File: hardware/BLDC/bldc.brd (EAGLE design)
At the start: 51 x 40 mm, 28 parts, among them U1 MA702, U2 DRV8323RS, U3 TPN7R006PL, U4 TPN7R006PL, U5 TPN7R006PL, U6 TPN7R006PL, U7 TPN7R006PL, U8 TPN7R006PL, U9 STM32G4_UFQFPN48_T1

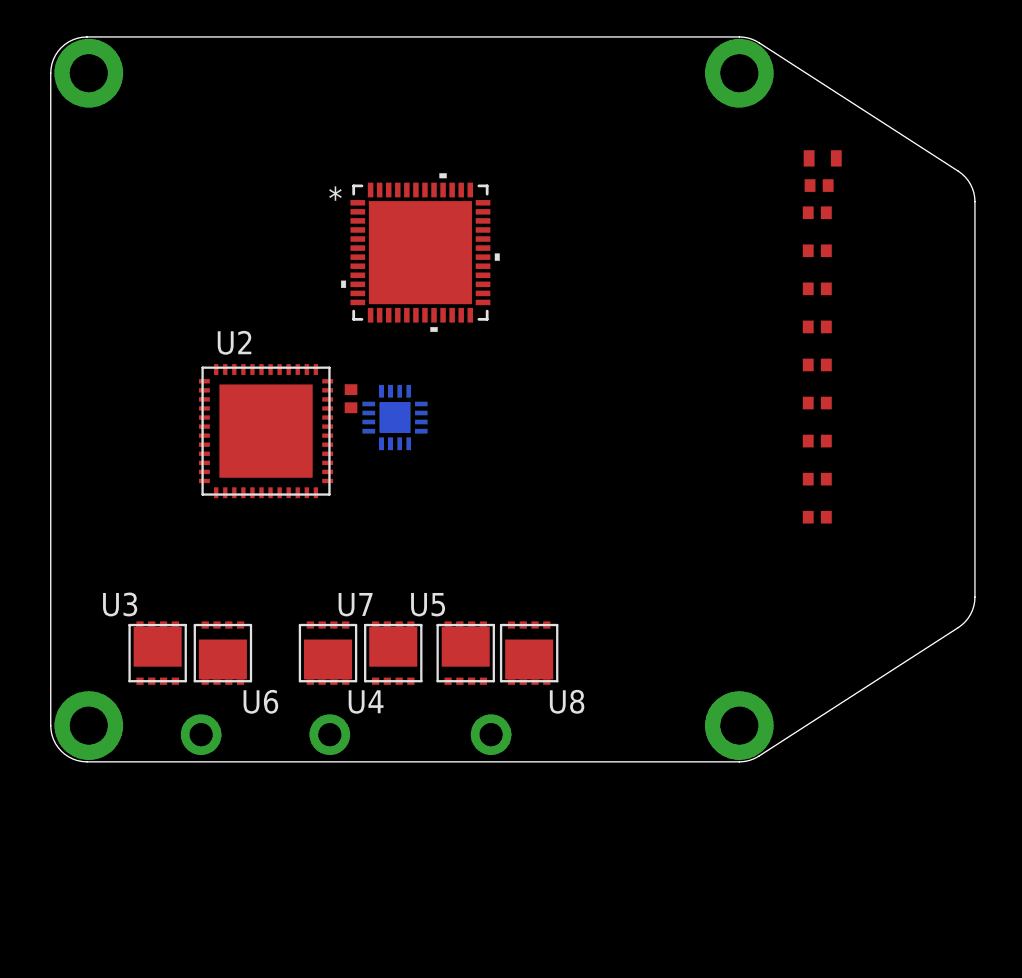
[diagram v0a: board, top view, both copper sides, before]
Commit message: Mostly updates to add inductor
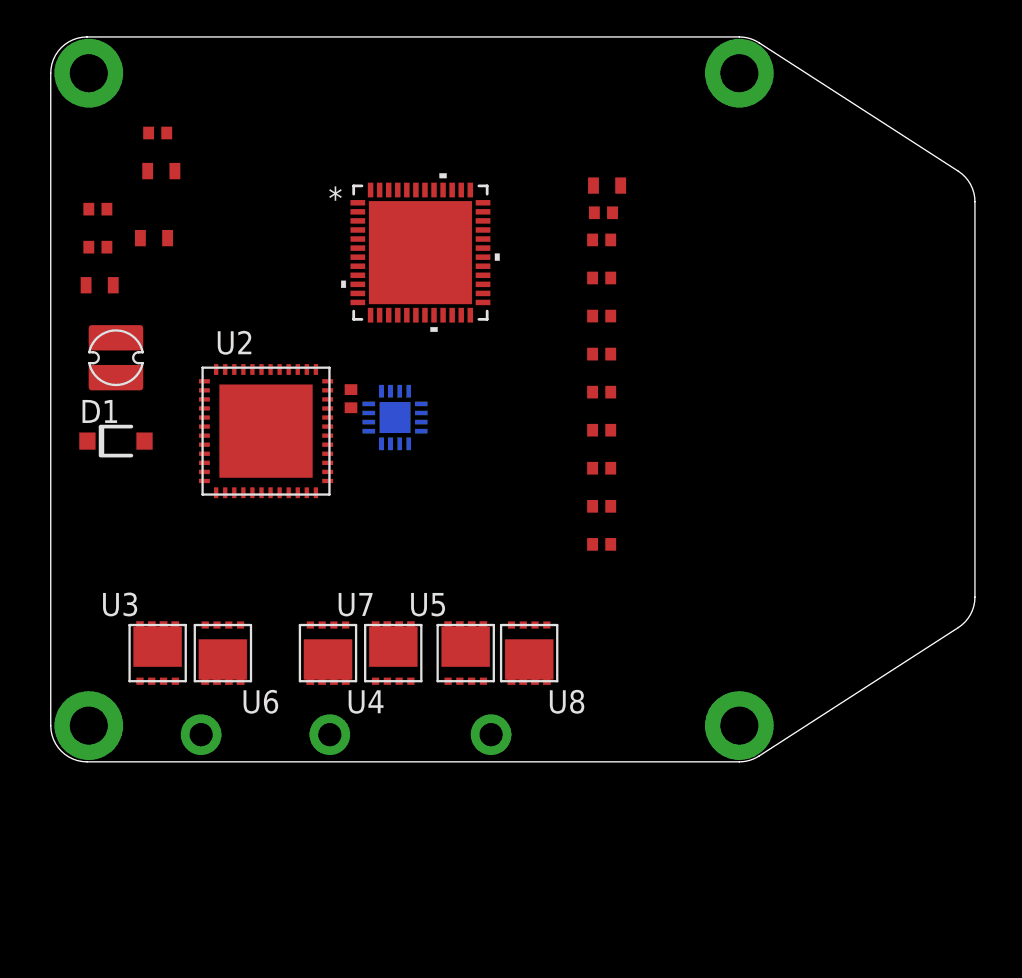
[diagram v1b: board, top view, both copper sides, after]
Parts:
- added C12, C14: 2.2uF 50V, _T_rcl:C0603
- added C13: 100nF 10V, _T_rcl:C0603
- added D1: SCHOTTKY_SOD123, _T_rcl:SOD123
- added L2: 22uH Bourns, _T_rcl:SDR0302
- added R1, R2, R3: 100k, _T_rcl:R0402
- moved L1 12.0 mm to (30.7, 31.8)
- moved C10 12.0 mm to (30.4, 14.1)
- moved C11 12.0 mm to (30.4, 12.0)
- moved C2 12.0 mm to (30.5, 30.3)
- moved C3 12.0 mm to (30.4, 28.8)
- moved C4 12.0 mm to (30.4, 26.7)
- moved C5 12.0 mm to (30.4, 24.6)
- moved C6 12.0 mm to (30.4, 22.5)
- moved C7 12.0 mm to (30.4, 20.4)
- moved C8 12.0 mm to (30.4, 18.3)
- moved C9 12.0 mm to (30.4, 16.2)
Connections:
- removed net GND: C1.2, C10.2, C11.2, C4.2, C5.2, C6.2, C7.2, C8.2, C9.2, H1.PAD, H2.PAD, H3.PAD, H4.PAD, U1.10, U1.8, U1.PAD, U2.38, U2.40, U2.42, U9.49
- new net N#8: C1.2, C10.2, C11.2, C12.2, C14.2, C4.2, C5.2, C6.2, C7.2, C8.2, C9.2, D1.A, H1.PAD, H2.PAD, H3.PAD, H4.PAD, R3.1, U1.10, U1.8, U1.PAD, U2.38, U2.40, U2.42, U2.43, U9.49
- new net N$10: C14.1, L2.PIN2, R2.2
- new net N$5: R1.2, U2.48
- new net N$6: C13.1, U2.44
- new net N$8: C13.2, D1.C, L2.PIN1, U2.45
- new net N$9: R2.1, R3.2, U2.1
- net +3V3: now also C12.1, R1.1, U2.47
- net N$2: now also U3.SOURCE, U3.SOURCE@1, U3.SOURCE@2, U6.DRAIN; no longer U3.PIN1, U3.PIN2, U3.PIN3, U6.PIN5, U6.PIN6, U6.PIN7, U6.PIN8
- net N$3: now also U4.SOURCE, U4.SOURCE@1, U4.SOURCE@2, U7.DRAIN; no longer U4.PIN1, U4.PIN2, U4.PIN3, U7.PIN5, U7.PIN6, U7.PIN7, U7.PIN8
- net N$4: now also U5.SOURCE, U5.SOURCE@1, U5.SOURCE@2, U8.DRAIN; no longer U5.PIN1, U5.PIN2, U5.PIN3, U8.PIN5, U8.PIN6, U8.PIN7, U8.PIN8

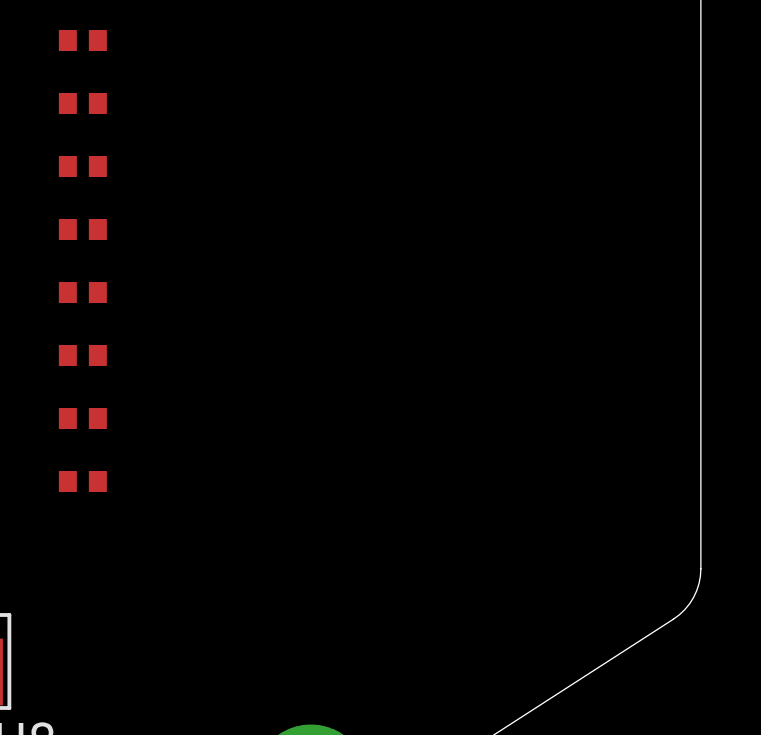
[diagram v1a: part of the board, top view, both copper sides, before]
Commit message: Added xt30
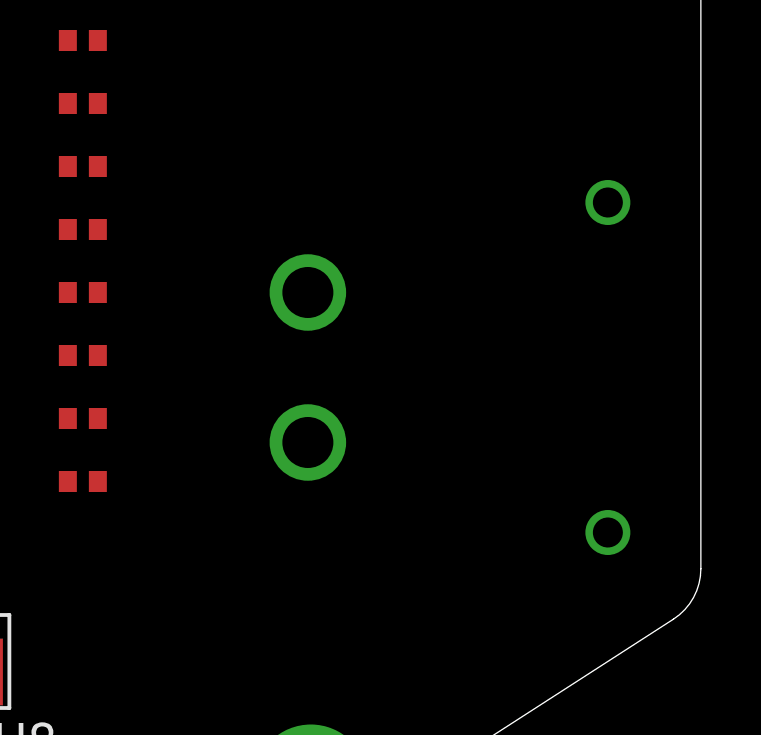
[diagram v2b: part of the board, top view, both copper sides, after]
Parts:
- added J1: PWR_2_XT30PW-M, _T_conn:XT30PW-M
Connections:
- new net +24V: C12.1, J1.P$1, R1.1, U2.47
- new net GND: J1.P$2
- net +3V3: no longer C12.1, R1.1, U2.47
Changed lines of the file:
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@@
 </layers>
 <board>
-<fusionsync huburn="a.YnVzaW5lc3M6Z21haWwyMjE5MTc" projecturn="a.YnVzaW5lc3M6Z21haWwyMjE5MTcjMjAxOTA2MjkyMDE0MTU5NzY" f3durn="urn:adsk.wipprod:dm.lineage:e4urj2y-ReajaBtUk_DaUw" pcbguid="" lastpulledtime="2020-05-16T20:54:00Z" lastsyncedchangeguid="" latestrevisionid="6bcccb4f-ea81-44fc-9b3c-a914c7c98af3" lastsyncedrevisionid="6bcccb4f-ea81-44fc-9b3c-a914c7c98af3" lastboardhashguid="70862e9e-f1a5-705a-7dcf-818cbcfc4620" lastpushedtime="2020-05-17T06:26:25Z" linktopcb3d="%12"/>
+<fusionsync huburn="a.YnVzaW5lc3M6Z21haWwyMjE5MTc" projecturn="a.YnVzaW5lc3M6Z21haWwyMjE5MTcjMjAxOTA2MjkyMDE0MTU5NzY" f3durn="urn:adsk.wipprod:dm.lineage:e4urj2y-ReajaBtUk_DaUw" pcbguid="" lastpulledtime="2020-05-16T20:54:00Z" lastsyncedchangeguid="" latestrevisionid="02e32407-8d36-474b-8d24-b2379baf0c01" lastsyncedrevisionid="02e32407-8d36-474b-8d24-b2379baf0c01" lastboardhashguid="b426c96d-69ff-6449-4c27-9cbcb447e0c3" lastpushedtime="2020-05-17T07:07:59Z" linktopcb3d="%12"/>
 <plain>
 <wire x1="39.0836" y1="39.681" x2="38" y2="40" width="0" layer="20" curve="32.8049"/>
@@
 </element>
 <element name="C1" library="_T_rcl" library_urn="urn:adsk.eagle:library:19571919" package="C0402" package3d_urn="urn:adsk.eagle:package:19572013/3" value="1uf 10v" x="16.57" y="20.04" smashed="yes" rot="R90"/>
-<element name="U4" library="_T_transistors" library_urn="urn:adsk.eagle:library:19605452" package="2-3X1S-TSONADVANCE" package3d_urn="urn:adsk.eagle:package:20292156/2" value="TPN7R006PL" x="15.3" y="6" smashed="yes" rot="R180">
+<element name="U4" library="_T_transistors" library_urn="urn:adsk.eagle:library:19605452" package="2-3X1S-TSONADVANCE" package3d_urn="urn:adsk.eagle:package:20292156/3" value="TPN7R006PL" x="15.3" y="6" smashed="yes" rot="R180">
 <attribute name="NAME" x="18.45" y="3.95" size="1.27" layer="25" rot="R180"/>
 <attribute name="VALUE" x="18.95" y="9.15" size="1.27" layer="27" rot="R180"/>
 </element>
-<element name="U5" library="_T_transistors" library_urn="urn:adsk.eagle:library:19605452" package="2-3X1S-TSONADVANCE" package3d_urn="urn:adsk.eagle:package:20292156/2" value="TPN7R006PL" x="22.9" y="6" smashed="yes">
+<element name="U5" library="_T_transistors" library_urn="urn:adsk.eagle:library:19605452" package="2-3X1S-TSONADVANCE" package3d_urn="urn:adsk.eagle:package:20292156/3" value="TPN7R006PL" x="22.9" y="6" smashed="yes">
 <attribute name="NAME" x="19.75" y="8.05" size="1.27" layer="25"/>
 <attribute name="VALUE" x="19.25" y="2.85" size="1.27" layer="27"/>
 </element>
-<element name="U6" library="_T_transistors" library_urn="urn:adsk.eagle:library:19605452" package="2-3X1S-TSONADVANCE" package3d_urn="urn:adsk.eagle:package:20292156/2" value="TPN7R006PL" x="9.5" y="6" smashed="yes" rot="R180">
+<element name="U6" library="_T_transistors" library_urn="urn:adsk.eagle:library:19605452" package="2-3X1S-TSONADVANCE" package3d_urn="urn:adsk.eagle:package:20292156/3" value="TPN7R006PL" x="9.5" y="6" smashed="yes" rot="R180">
 <attribute name="NAME" x="12.65" y="3.95" size="1.27" layer="25" rot="R180"/>
 <attribute name="VALUE" x="13.15" y="9.15" size="1.27" layer="27" rot="R180"/>
 </element>
-<element name="U7" library="_T_transistors" library_urn="urn:adsk.eagle:library:19605452" package="2-3X1S-TSONADVANCE" package3d_urn="urn:adsk.eagle:package:20292156/2" value="TPN7R006PL" x="18.9" y="6" smashed="yes">
+<element name="U7" library="_T_transistors" library_urn="urn:adsk.eagle:library:19605452" package="2-3X1S-TSONADVANCE" package3d_urn="urn:adsk.eagle:package:20292156/3" value="TPN7R006PL" x="18.9" y="6" smashed="yes">
 <attribute name="NAME" x="15.75" y="8.05" size="1.27" layer="25"/>
 <attribute name="VALUE" x="15.25" y="2.85" size="1.27" layer="27"/>
 </element>
-<element name="U8" library="_T_transistors" library_urn="urn:adsk.eagle:library:19605452" package="2-3X1S-TSONADVANCE" package3d_urn="urn:adsk.eagle:package:20292156/2" value="TPN7R006PL" x="26.4" y="6" smashed="yes" rot="R180">
+<element name="U8" library="_T_transistors" library_urn="urn:adsk.eagle:library:19605452" package="2-3X1S-TSONADVANCE" package3d_urn="urn:adsk.eagle:package:20292156/3" value="TPN7R006PL" x="26.4" y="6" smashed="yes" rot="R180">
 <attribute name="NAME" x="29.55" y="3.95" size="1.27" layer="25" rot="R180"/>
 <attribute name="VALUE" x="30.05" y="9.15" size="1.27" layer="27" rot="R180"/>
@@
 <element name="R1" library="_T_rcl" library_urn="urn:adsk.eagle:library:19571919" package="R0402" package3d_urn="urn:adsk.eagle:package:19572014/2" value="100k" x="5.9" y="34.7" smashed="yes"/>
 <element name="C13" library="_T_rcl" library_urn="urn:adsk.eagle:library:19571919" package="C0603" package3d_urn="urn:adsk.eagle:package:19572011/2" value="100nF 10V" x="6.1" y="32.6" smashed="yes"/>
-<element name="L2" library="_T_rcl" library_urn="urn:adsk.eagle:library:19571919" package="SDR0302" package3d_urn="urn:adsk.eagle:package:20294118/3" value="22uH Bourns" x="3.6" y="22.3" smashed="yes"/>
+<element name="L2" library="_T_rcl" library_urn="urn:adsk.eagle:library:19571919" package="SDR0302" package3d_urn="urn:adsk.eagle:package:20294118/4" value="22uH Bourns" x="3.6" y="22.3" smashed="yes"/>
 <element name="R2" library="_T_rcl" library_urn="urn:adsk.eagle:library:19571919" package="R0402" package3d_urn="urn:adsk.eagle:package:19572014/2" value="100k" x="2.6" y="30.5" smashed="yes"/>
 <element name="R3" library="_T_rcl" library_urn="urn:adsk.eagle:library:19571919" package="R0402" package3d_urn="urn:adsk.eagle:package:19572014/2" value="100k" x="2.6" y="28.4" smashed="yes"/>
 <element name="C14" library="_T_rcl" library_urn="urn:adsk.eagle:library:19571919" package="C0603" package3d_urn="urn:adsk.eagle:package:19572011/2" value="2.2uF 50V" x="2.7" y="26.3" smashed="yes"/>
-<element name="D1" library="_T_rcl" library_urn="urn:adsk.eagle:library:19571919" package="SOD123" package3d_urn="urn:adsk.eagle:package:20295471/1" value="SCHOTTKY_SOD123" x="3.6" y="17.7" smashed="yes">
+<element name="D1" library="_T_rcl" library_urn="urn:adsk.eagle:library:19571919" package="SOD123" package3d_urn="urn:adsk.eagle:package:20295471/2" value="SCHOTTKY_SOD123" x="3.6" y="17.7" smashed="yes">
 <attribute name="NAME" x="1.6" y="18.7" size="1.27" layer="25"/>
 <attribute name="VALUE" x="1.6" y="15.2" size="1.27" layer="27"/>
 </element>
-<element name="U3" library="_T_transistors" library_urn="urn:adsk.eagle:library:19605452" package="2-3X1S-TSONADVANCE" package3d_urn="urn:adsk.eagle:package:20292156/2" value="TPN7R006PL" x="5.9" y="6" smashed="yes">
+<element name="U3" library="_T_transistors" library_urn="urn:adsk.eagle:library:19605452" package="2-3X1S-TSONADVANCE" package3d_urn="urn:adsk.eagle:package:20292156/3" value="TPN7R006PL" x="5.9" y="6" smashed="yes">
 <attribute name="NAME" x="2.75" y="8.05" size="1.27" layer="25"/>
 <attribute name="VALUE" x="2.25" y="2.85" size="1.27" layer="27"/>
 </element>
+<element name="J1" library="_T_conn" library_urn="urn:adsk.eagle:library:19570503" package="XT30PW-M" package3d_urn="urn:adsk.eagle:package:20295844/2" value="PWR_2_XT30PW-M" x="47.9" y="15.8" smashed="yes" rot="MR270"/>
 </elements>
 <signals>
@@
 <contactref element="C11" pad="1"/>
 <contactref element="C10" pad="1"/>
-<contactref element="C12" pad="1"/>
-<contactref element="U2" pad="47"/>
-<contactref element="R1" pad="1"/>
 <wire x1="30.9" y1="26.7" x2="31.45" y2="31.8" width="0" layer="19" extent="1-1"/>
 <wire x1="30.9" y1="24.6" x2="30.9" y2="26.7" width="0" layer="19" extent="1-1"/>
@@
 <wire x1="30.9" y1="14.1" x2="30.9" y2="16.2" width="0" layer="19" extent="1-1"/>
 <wire x1="30.9" y1="12" x2="30.9" y2="14.1" width="0" layer="19" extent="1-1"/>
-<wire x1="23.8544" y1="30.35" x2="30.9" y2="26.7" width="0" layer="19" extent="1-1"/>
+<wire x1="23.8544" y1="30.35" x2="31.45" y2="31.8" width="0" layer="19" extent="1-1"/>
 <wire x1="22.65" y1="24.6456" x2="23.8544" y2="30.35" width="0" layer="19" extent="1-1"/>
 <wire x1="21.65" y1="24.6456" x2="22.65" y2="24.6456" width="0" layer="19" extent="1-1"/>
@@
 <wire x1="17.65" y1="31.5544" x2="23.8544" y2="30.35" width="0" layer="19" extent="1-1"/>
 <wire x1="16.9456" y1="30.85" x2="17.65" y2="31.5544" width="0" layer="19" extent="1-1"/>
-<wire x1="9.63" y1="21.65" x2="16.57" y2="20.54" width="0" layer="19" extent="1-1"/>
-<wire x1="6.45" y1="28.9" x2="9.63" y2="21.65" width="0" layer="19" extent="1-1"/>
-<wire x1="6.4" y1="34.7" x2="6.45" y2="28.9" width="0" layer="19" extent="1-1"/>
 </signal>
 <signal name="N$1">
@@
 <wire x1="3.6" y1="21.275" x2="3.45" y2="26.3" width="0" layer="19" extent="1-1"/>
 </signal>
+<signal name="GND">
+<contactref element="J1" pad="P$2"/>
+</signal>
+<signal name="+24V">
+<contactref element="C12" pad="1"/>
+<contactref element="U2" pad="47"/>
+<contactref element="R1" pad="1"/>
+<contactref element="J1" pad="P$1"/>
+<wire x1="9.63" y1="21.65" x2="37.9" y2="18.3" width="0" layer="19" extent="1-1"/>
+<wire x1="6.45" y1="28.9" x2="9.63" y2="21.65" width="0" layer="19" extent="1-1"/>
+<wire x1="6.4" y1="34.7" x2="6.45" y2="28.9" width="0" layer="19" extent="1-1"/>
+</signal>
 </signals>

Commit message: Added bulk caps
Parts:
- added C15, C16, C17, C18, C19, C20, C21, C22, C23, C24, C25, C26, C27, C28, C29, C30: 10uF V50, _T_rcl:C1206
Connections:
- net +24V: now also C15.1, C16.1, C17.1, C18.1, C19.1, C20.1, C21.1, C22.1, C23.1, C24.1, C25.1, C26.1, C27.1, C28.1, C29.1, C30.1
- net GND: now also C15.2, C16.2, C17.2, C18.2, C19.2, C20.2, C21.2, C22.2, C23.2, C24.2, C25.2, C26.2, C27.2, C28.2, C29.2, C30.2
